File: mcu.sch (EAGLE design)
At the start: 64 parts, among them IC1 MCP73831/OT, T1 SI7051-A20, U4 NRF52832, U7 CP2102N-A01-GQFN24, X1 LFXTAL069526, X6 32.768kHz

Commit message: UPD: finishied version to macrofab
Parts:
- removed GND: (no value), microbuilder:TESTPOINTROUND2MM
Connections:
- net GND: no longer GND.P$1
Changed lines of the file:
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@@
 <part name="SWDCLK" library="microbuilder" deviceset="TESTPOINT" device="ROUND2MM"/>
 <part name="SWDIO" library="microbuilder" deviceset="TESTPOINT" device="ROUND2MM"/>
-<part name="GND" library="microbuilder" deviceset="TESTPOINT" device="ROUND2MM"/>
 <part name="SWO" library="microbuilder" deviceset="TESTPOINT" device="ROUND2MM"/>
 <part name="GND12" library="supply1" deviceset="GND" device=""/>
@@
 <instance part="SWDCLK" gate="G$1" x="259.08" y="190.5" rot="R90"/>
 <instance part="SWDIO" gate="G$1" x="259.08" y="200.66" rot="R90"/>
-<instance part="GND" gate="G$1" x="259.08" y="167.64" rot="R90"/>
 <instance part="SWO" gate="G$1" x="259.08" y="208.28" rot="R90"/>
 <instance part="GND12" gate="1" x="213.36" y="116.84"/>
@@
 </segment>
 <segment>
-<pinref part="GND" gate="G$1" pin="P$1"/>
-<wire x1="259.08" y1="167.64" x2="261.62" y2="167.64" width="0.1524" layer="91"/>
-<label x="261.62" y="167.64" size="1.778" layer="95" xref="yes"/>
-</segment>
-<segment>

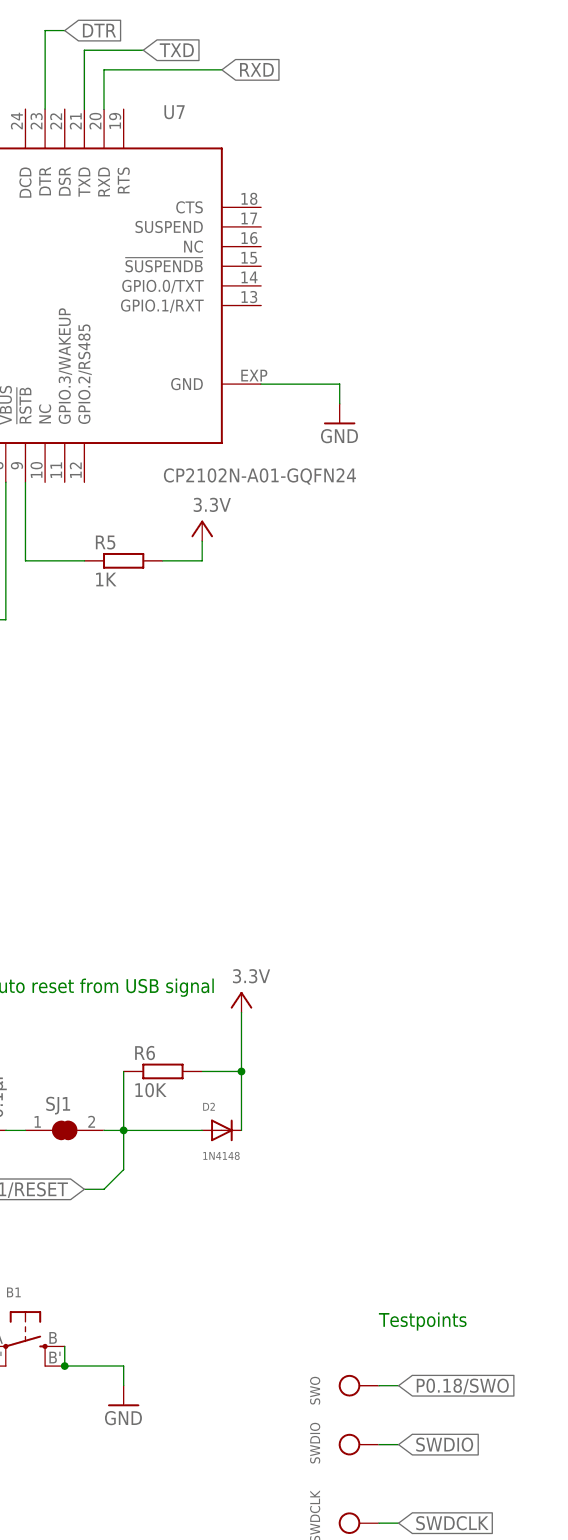
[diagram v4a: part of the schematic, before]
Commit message: FIX: txd, rxd lines, usb. UPD: testpoints.
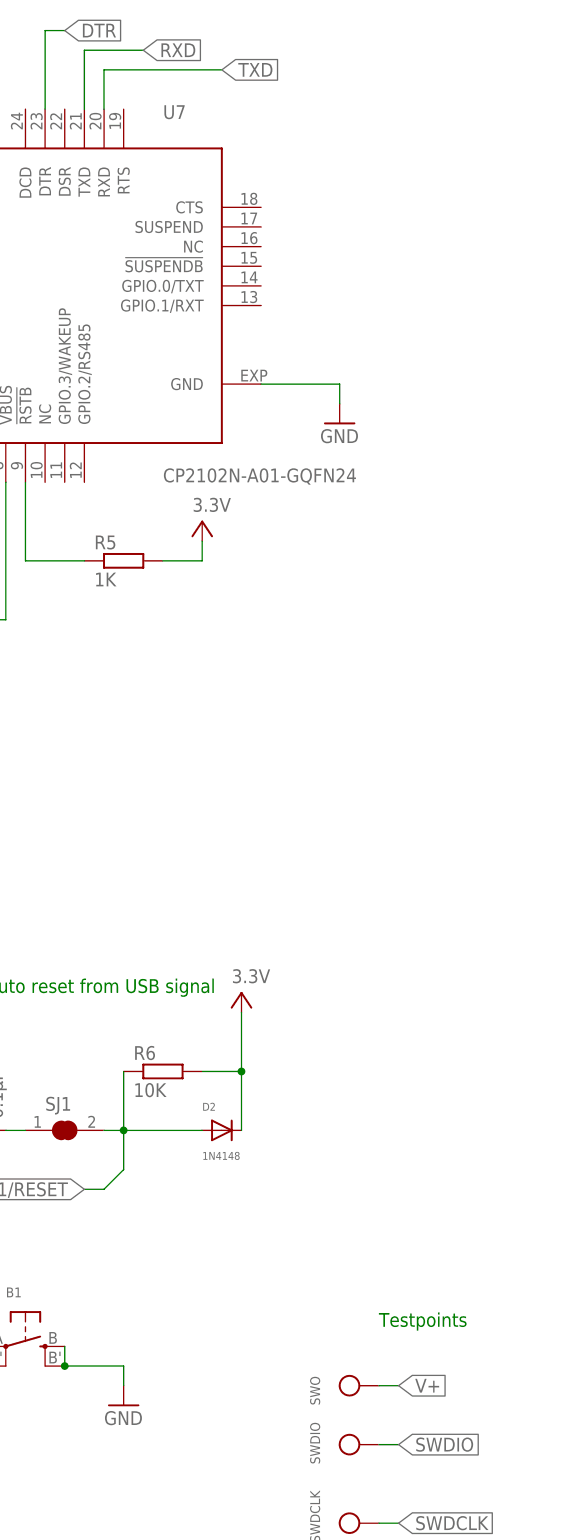
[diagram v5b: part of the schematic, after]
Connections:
- net P0.18/SWO: no longer SWO.P$1
- net RXD: now also U7.TXD; no longer U7.RXD
- net TXD: now also U7.RXD; no longer U7.TXD
- net V+: now also SWO.P$1
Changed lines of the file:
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@@
 <?xml version="1.0" encoding="utf-8"?>
 <!DOCTYPE eagle SYSTEM "eagle.dtd">
-<eagle version="8.5.2">
+<eagle version="8.6.3">
 <drawing>
 <settings>
@@
 </segment>
 <segment>
+<pinref part="U7" gate="CP2102N-A01-GQFN24" pin="RXD"/>
+<wire x1="223.52" y1="373.38" x2="223.52" y2="378.46" width="0.1524" layer="91"/>
+<label x="238.76" y="378.46" size="1.778" layer="95" xref="yes"/>
+<wire x1="223.52" y1="378.46" x2="238.76" y2="378.46" width="0.1524" layer="91"/>
+</segment>
+</net>
+<net name="P0.07" class="0">
+<segment>
+<wire x1="38.1" y1="220.98" x2="35.56" y2="220.98" width="0.1524" layer="91"/>
+<label x="35.56" y="220.98" size="1.27" layer="95" rot="R180" xref="yes"/>
+<pinref part="U4" gate="U$1" pin="P0.07@09"/>
+</segment>
+</net>
+<net name="RXD" class="0">
+<segment>
+<wire x1="38.1" y1="218.44" x2="35.56" y2="218.44" width="0.1524" layer="91"/>
+<label x="35.56" y="218.44" size="1.27" layer="95" rot="R180" xref="yes"/>
+<pinref part="U4" gate="U$1" pin="P0.08@10"/>
+</segment>
+<segment>
 <pinref part="U7" gate="CP2102N-A01-GQFN24" pin="TXD"/>
 <wire x1="220.98" y1="373.38" x2="220.98" y2="381" width="0.1524" layer="91"/>
@@
 </segment>
 </net>
-<net name="P0.07" class="0">
-<segment>
-<wire x1="38.1" y1="220.98" x2="35.56" y2="220.98" width="0.1524" layer="91"/>
-<label x="35.56" y="220.98" size="1.27" layer="95" rot="R180" xref="yes"/>
-<pinref part="U4" gate="U$1" pin="P0.07@09"/>
-</segment>
-</net>
-<net name="RXD" class="0">
-<segment>
-<wire x1="38.1" y1="218.44" x2="35.56" y2="218.44" width="0.1524" layer="91"/>
-<label x="35.56" y="218.44" size="1.27" layer="95" rot="R180" xref="yes"/>
-<pinref part="U4" gate="U$1" pin="P0.08@10"/>
-</segment>
-<segment>
-<pinref part="U7" gate="CP2102N-A01-GQFN24" pin="RXD"/>
-<wire x1="223.52" y1="373.38" x2="223.52" y2="378.46" width="0.1524" layer="91"/>
-<label x="238.76" y="378.46" size="1.778" layer="95" xref="yes"/>
-<wire x1="223.52" y1="378.46" x2="238.76" y2="378.46" width="0.1524" layer="91"/>
-</segment>
-</net>
 <net name="P0.09" class="0">
 <segment>
@@
 <label x="76.2" y="193.04" size="1.27" layer="95" rot="R270" xref="yes"/>
 <pinref part="U4" gate="U$1" pin="P0.18/SWO@21"/>
-</segment>
-<segment>
-<pinref part="SWO" gate="G$1" pin="P$1"/>
-<wire x1="259.08" y1="208.28" x2="261.62" y2="208.28" width="0.1524" layer="91"/>
-<label x="261.62" y="208.28" size="1.778" layer="95" xref="yes"/>
 </segment>
 </net>
@@
 <wire x1="-81.28" y1="124.46" x2="-81.28" y2="129.54" width="0.1524" layer="91"/>
 </segment>
-</net>
+<segment>
+<pinref part="SWO" gate="G$1" pin="P$1"/>
+<wire x1="259.08" y1="208.28" x2="261.62" y2="208.28" width="0.1524" layer="91"/>
+<label x="261.62" y="208.28" size="1.778" layer="95" xref="yes"/>
+</segment>
+</net>

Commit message: FIX: usb connections
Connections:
- net USBD+: now also USB1.3; no longer USB1.2
- net USBD-: now also USB1.2; no longer USB1.3
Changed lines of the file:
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@@
 <?xml version="1.0" encoding="utf-8"?>
 <!DOCTYPE eagle SYSTEM "eagle.dtd">
-<eagle version="8.6.3">
+<eagle version="8.6.1">
 <drawing>
 <settings>
@@
 <instance part="D1" gate="NRVB120VLSF" x="-76.2" y="345.44"/>
 <instance part="USB1" gate="ZX62R-B-5P(30)" x="45.72" y="355.6"/>
-<instance part="GND5" gate="1" x="40.64" y="345.44"/>
-<instance part="U$4" gate="G$2" x="58.42" y="345.44"/>
+<instance part="GND5" gate="1" x="50.8" y="345.44"/>
+<instance part="U$4" gate="G$2" x="35.56" y="350.52"/>
 <instance part="IC1" gate="G$1" x="111.76" y="347.98"/>
 <instance part="U$5" gate="G$2" x="73.66" y="363.22"/>
@@
 <pinref part="USB1" gate="ZX62R-B-5P(30)" pin="5"/>
 <pinref part="GND5" gate="1" pin="GND"/>
-<wire x1="40.64" y1="353.06" x2="40.64" y2="347.98" width="0.1524" layer="91"/>
+<wire x1="50.8" y1="353.06" x2="50.8" y2="347.98" width="0.1524" layer="91"/>
 </segment>
 <segment>
@@
 <net name="USBD-" class="0">
 <segment>
-<pinref part="USB1" gate="ZX62R-B-5P(30)" pin="3"/>
-<wire x1="45.72" y1="353.06" x2="45.72" y2="335.28" width="0.1524" layer="91"/>
-<label x="45.72" y="335.28" size="1.778" layer="95" rot="R180" xref="yes"/>
-</segment>
-<segment>
 <pinref part="U7" gate="CP2102N-A01-GQFN24" pin="D-"/>
 <label x="180.34" y="353.06" size="1.778" layer="95" rot="R180" xref="yes"/>
 <wire x1="195.58" y1="353.06" x2="180.34" y2="353.06" width="0.1524" layer="91"/>
 </segment>
+<segment>
+<pinref part="USB1" gate="ZX62R-B-5P(30)" pin="2"/>
+<wire x1="43.18" y1="353.06" x2="43.18" y2="330.2" width="0.1524" layer="91"/>
+<label x="43.18" y="330.2" size="1.778" layer="95" rot="R180" xref="yes"/>
+</segment>
 </net>
 <net name="USBD+" class="0">
-<segment>
-<pinref part="USB1" gate="ZX62R-B-5P(30)" pin="2"/>
-<wire x1="48.26" y1="353.06" x2="48.26" y2="327.66" width="0.1524" layer="91"/>
-<label x="48.26" y="327.66" size="1.778" layer="95" rot="R180" xref="yes"/>
-</segment>
 <segment>
 <pinref part="U7" gate="CP2102N-A01-GQFN24" pin="D+"/>
 <wire x1="195.58" y1="355.6" x2="193.04" y2="355.6" width="0.1524" layer="91"/>
 <label x="193.04" y="355.6" size="1.778" layer="95" rot="R180" xref="yes"/>
+</segment>
+<segment>
+<pinref part="USB1" gate="ZX62R-B-5P(30)" pin="3"/>
+<wire x1="45.72" y1="353.06" x2="45.72" y2="335.28" width="0.1524" layer="91"/>
+<label x="45.72" y="335.28" size="1.778" layer="95" xref="yes"/>
 </segment>
 </net>
@@
 <segment>
 <pinref part="U$4" gate="G$2" pin="VUSB"/>
-<wire x1="58.42" y1="342.9" x2="58.42" y2="337.82" width="0.1524" layer="91"/>
-<wire x1="58.42" y1="337.82" x2="50.8" y2="337.82" width="0.1524" layer="91"/>
+<wire x1="35.56" y1="347.98" x2="35.56" y2="340.36" width="0.1524" layer="91"/>
+<wire x1="35.56" y1="340.36" x2="40.64" y2="340.36" width="0.1524" layer="91"/>
 <pinref part="USB1" gate="ZX62R-B-5P(30)" pin="1"/>
-<wire x1="50.8" y1="337.82" x2="50.8" y2="353.06" width="0.1524" layer="91"/>
-</segment>
-<segment>
+<wire x1="40.64" y1="340.36" x2="40.64" y2="353.06" width="0.1524" layer="91"/>
+</segment>
+<segment>

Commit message: UPD: v2 wiring complete
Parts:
- removed B1: (no value), microbuilder:SWITCH_TACT_SMT4.6X2.8
- removed C10, C6, C8: 0.1µF, rcl:C-EUC0603K
- removed C38: DNP, Nordic_nRF:CAPACITOR_0402_N
- removed C5: 4.7µF, rcl:C-EUC0603
- removed C9: 1nF, rcl:C-EUC0603
- removed LDO1: AP2112-3.3K, tilesPartComp:AP2112-3.3K
- removed LED1: Orange, microbuilder:LED0805
- removed R10, R14: 22, rcl:R-EU_R0603
- removed R12: 2M, rcl:R-EU_R0603
- removed R13: 100, rcl:R-EU_R0603
- removed R15: 10K, rcl:R-EU_R0603
- removed R16: 0, rcl:R-EU_R0402
- removed R17, R18: DNP, rcl:R-EU_R0402
- removed RGB1: 150080M153000, tilesPartComp:150080M153000
- removed SJ1: (no value), microbuilder:SOLDERJUMPER_CLOSED
- removed TEST1, TEST2: TESTPOINT_SQUARE_SMT, tilesPartComp:TESTPOINT_SQUARE_SMT
- removed U7: CP2102N-A01-GQFN24, tilesPartComp:CP2102N-A01-GQFN24
- added BAT+, BAT-: (no value), microbuilder:TESTPOINTROUND2MM
- added C7: 10uF, MF_Passives:CAPACITOR_NP_0603
- added D3: MF-LED-0603-RED, MF_LEDs:LED_SINGLE-0603-RED
- added R7: 100K, MF_Passives:RESISTOR_0402
- added R8: 100, MF_Passives:RESISTOR_0402
- added SW1: MF-SW-TACT-4.2MM, MF_Switches:TACT_4.2MM
- added U1: MF-REG-SOT235-3.3V-300mA, MF_IC_Power:TLV70233PDBVR
- C1, C2: value 10µF -> 10uF; device rcl:C-EUC0805 -> MF_Passives:CAPACITOR_NP_0603; MPN (none) -> JMK107ABJ106KA-T
- C3: value 10µF -> 0.1uF; device rcl:C-EUC0805 -> MF_Passives:CAPACITOR_NP_0402; HOUSEPART (none) -> YES; MPN (none) -> MF-CAP-0402-0.1uF
- C4: value 0.1µF -> 0.1uF; device rcl:C-EUC0603K -> MF_Passives:CAPACITOR_NP_0402; HOUSEPART (none) -> YES; MPN (none) -> MF-CAP-0402-0.1uF
- D1: value NRVB120VLSF -> MF-DIO-SMA-B140; device tilesPartComp:NRVB120VLSF -> MF_Discrete_Semiconductor:DIODES_B140_SMA
- D2: value 1N4148 -> MF-LED-3228-RGB; device tilesPartComp:1N4148W-7-F -> MF_LEDs:LED_RGB_CA_PLCC4
- R1: device rcl:R-EU_R0603 -> MF_Passives:RESISTOR_0402; HOUSEPART (none) -> YES; MPN (none) -> MF-RES-0402-100K
- R11: value 806K -> 22; device rcl:R-EU_R0603 -> MF_Passives:RESISTOR_0402; HOUSEPART (none) -> YES; MPN (none) -> MF-RES-0402-22
- R2: value 100K -> 560; device rcl:R-EU_R0603 -> MF_Passives:RESISTOR_0402; HOUSEPART (none) -> YES; MPN (none) -> MF-RES-0402-560
- R3: value 200 -> 18K; device rcl:R-EU_R0603 -> MF_Passives:RESISTOR_0402; HOUSEPART (none) -> YES; MPN (none) -> MF-RES-0402-18K
- R4: value 37K -> 18K; device rcl:R-EU_R0603 -> MF_Passives:RESISTOR_0402; HOUSEPART (none) -> YES; MPN (none) -> MF-RES-0402-18K
- R5: value 1K -> 10K; device rcl:R-EU_R0603 -> MF_Passives:RESISTOR_0402; HOUSEPART (none) -> YES; MPN (none) -> MF-RES-0402-10K
- R6: device rcl:R-EU_R0603 -> MF_Passives:RESISTOR_0402; HOUSEPART (none) -> YES; MPN (none) -> MF-RES-0402-10K
- R9: value 10K -> 22; device rcl:R-EU_R0603 -> MF_Passives:RESISTOR_0402; HOUSEPART (none) -> YES; MPN (none) -> MF-RES-0402-22
- renumbered SWO to VDD
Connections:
- removed net DTR: C6.1, U7.DTR
- removed net N$18: ANT1.1, R16.2, R17.2
- removed net N$19: R13.2, RGB1.R
- removed net N$20: R10.2, RGB1.G
- removed net N$21: R14.2, RGB1.B
- new net N$13: R3.P$2, R4.P$1
- new net N$14: D2.CATHODE_BLUE, R11.P$1
- net DEC2: no longer C38.1
- net GND: now also BAT-.P$1, C1.P$2, C2.P$2, C3.P$2, C4.P$2, C7.P$2, R4.P$2, R7.P$2, SW1.P$1, SW1.P$2, U1.GND/ADJ; no longer B1.S, B1.S1, C1.2, C10.2, C2.2, C3.2, C38.2, C4.2, C5.2, C8.2, C9.1, LDO1.GND, R12.1, R17.1, R18.1, R2.2, R4.2, TEST2.P, U7.GND, U7.GND@EXP
- net N$1: now also R1.P$2, U1.EN; no longer LDO1.EN, R1.1
- net N$2: now also C7.P$1, D1.CATHODE, R1.P$1, U1.VIN; no longer C2.1, D1.C, LDO1.VIN, R1.2
- net N$3: now also R2.P$2; no longer R3.2
- net N$4: now also D3.CATHODE, R2.P$1; no longer LED1.C, R3.1
- net N$5: now also D2.CATHODE_RED, R8.P$1; no longer R5.1, U7.!RSTB
- net N$6: now also R3.P$1; no longer R4.1
- net N$7: now also D2.CATHODE_GREEN, R9.P$1; no longer C6.2, SJ1.1
- net P0.02: now also R8.P$2; no longer R13.1
- net P0.03: now also R9.P$2; no longer R10.1
- net P0.04: now also R11.P$2; no longer R14.1
- net P0.21/RESET: now also SW1.P$3, SW1.P$4; no longer B1.P, B1.P1, D2.A, R6.1, SJ1.2
- net P0.25: now also R6.P$2; no longer R15.1
- net P0.26: now also R5.P$2; no longer R9.1
- net P0.31: no longer C9.2, R11.1, R12.2
- net RF: now also ANT1.1; no longer R16.1, R18.2
- net RXD: no longer U7.TXD
- net TXD: no longer U7.RXD
- net USBD+: no longer U7.D+
- net USBD-: no longer U7.D-
- net V+: now also C1.P$1, C3.P$1, C4.P$1, D2.ANODE, R5.P$1, R6.P$1, U1.VOUT; no longer C1.1, C10.1, C4.1, C5.1, C8.1, D2.C, LDO1.VOUT, R15.2, R5.2, R6.2, R9.2, RGB1.VDD, U7.VDD, U7.VIO, U7.VREGIN
- net VBAT: now also BAT+.P$1, C2.P$1; no longer C3.1, R11.2, TEST1.P
- net VUSB: now also D1.ANODE, D3.ANODE, R7.P$1; no longer D1.A, LED1.A, R2.1, U7.VBUS
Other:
- note added: "36K = 28mA"
- note added: "DNP capacitor"
- note removed: "37K = 27mA"
- note removed: "Auto reset from USB signal"
- note removed: "LIPO MONITORING"
- note removed: "See: https://devzone.nordicsemi.com/blogs/943/measuring-lithium-battery-voltage-with-nrf52/ Maximum voltage: 4.2 V * (2 M/(0.8 M+2 M)) = 3 V Minimum voltage: 2.7 V * (2 M/(0.8 M+2 M)) = 1.93 V ADC value at 4.2 V - 12 bit setup: 3 V * (1/5) / 0.6 V * 4095 = 4095 ADC value at 2.7 V - 12 bit setup: 1.93 V * (1/5) / 0.6 V * 4095 = 2634 Usable ADC resolution - 12 bit setup: 4095 - 2634 = 1461"
- moved on the sheet: ANT1

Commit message: UPD: design and components
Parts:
- removed C36, C37, C40: 100nF, Nordic_nRF:CAPACITOR_0402_N
- removed C42: 1.0µF, Nordic_nRF:CAPACITOR_0603_N
- removed L9: 10µH, Nordic_nRF:INDUCTOR_0603_N
- added C5, C6, C8: 0.1uF, MF_Passives:CAPACITOR_NP_0402
- added C9: 1.0uF, MF_Passives:CAPACITOR_NP_0603
- added L1: 10uH, MF_Passives:INDUCTOR_1210
- ANT1: MPN (none) -> 2450AT45A100E
- C1, C2, C7: HOUSEPART (none) -> YES
- C33, C34, C43, C44: MPN (none) -> C0402C120J5GACTU
- C39: MPN (none) -> GRM1555C1H101GA01D
- C41: MPN (none) -> 06036D475KAT2A
- F1: MPN (none) -> 2450FM07A0029T
- HU1: MPN (none) -> HDC2010YPAR
- IC1: MPN (none) -> MCP73831T-2ACI/OT
- L10: MPN (none) -> L-07C15NJV6T
- MOS1: MPN (none) -> DMG3415U-7
- T1: MPN (none) -> SI7051-A20-IM
- U4: MPN (none) -> NRF52832-QFAA-R7
- USB1: MPN (none) -> ZX62R-B-5P(30)
- X1: MPN (none) -> LFXTAL069526CUTT
- X6: MPN (none) -> LFXTAL009706REEL
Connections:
- net DEC1: now also C5.P$1; no longer C36.1
- net DEC4: now also C9.P$1; no longer C42.1
- net GND: now also C5.P$2, C6.P$2, C8.P$2, C9.P$2; no longer C36.2, C37.2, C40.2, C42.2
- net N$10: now also L1.P$1; no longer L9.1
- net N$9: now also L1.P$2; no longer L9.2
- net V+: now also C6.P$1, C8.P$1; no longer C37.1, C40.1
